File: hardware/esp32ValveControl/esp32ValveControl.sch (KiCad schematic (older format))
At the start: 65 parts, among them Q1 BSS138, Q2 BSS138, Q5 BSS138, Q7 BSS138, SW2 Reset, U1 ESP32-WROOM, U2 AQY212, U3 AQY212, U4 MC34063, U5 MOCD207M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

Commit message: schem_/pcb update
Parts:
- removed D1, D2, D3: LED, LEDs:LED-0603, symbol device:LED
- added C1: 100n, Capacitors_SMD:C_0603, symbol device:C_Small
- added P1: CONN_01X05, Pin_Headers:Pin_Header_Straight_1x05_Pitch2.54mm, symbol conn:CONN_01X05
- added R23: 100, Resistors_SMD:R_0603, symbol device:R
- added SW1: Boot, switches:SMD_Switch_6.5x6, symbol standard:Switch_4P
- added U8: MOCD207M, Housings_SOIC:SOIC-8_3.9x4.9mm_Pitch1.27mm, symbol opto:PC827
- R18, R19, R22, R3, R4, R5: value 470 -> 10k
- R20, R21: value 470 -> tbd
- R8, R9: value 33 -> 10k
- U2, U3, U6, U7: footprint DIP-4-SMD -> Housings_DIP:DIP-4_W7.62mm_SMDSocket_SmallPads
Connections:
- net labels added: IN3, IN4, OPTO3, OPTO4, VCOM, nBoot
- net labels removed: PA12, PA13, PA14, PD6, PD7, PE0, PE1
- wire segments 99 -> 129
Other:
- moved on the sheet: SW2

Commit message: hardware update
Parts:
- removed U5, U8: MOCD207M, Housings_SOIC:SOIC-8_3.9x4.9mm_Pitch1.27mm, symbol opto:PC827
- added U10, U5, U8, U9: LTV-354T, SOIC_Packages:SO-4_4.4x3.6mm_Pitch2.54mm, symbol Isolator:LTV-354T
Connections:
- wire segments 129 -> 137
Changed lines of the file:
@@
-$EndComp
-$Comp
-L opto:PC827 U5
-U 1 1 571AB759
-P 1600 3400
-F 0 "U5" H 1400 3600 50  0000 L CNN
-F 1 "MOCD207M" H 1600 3600 50  0000 L CNN
-F 2 "Housings_SOIC:SOIC-8_3.9x4.9mm_Pitch1.27mm" H 1400 3200 50  0001 L CIN
-F 3 "" H 1600 3400 50  0000 L CNN
-	1    1600 3400
-	1    0    0    -1
-$EndComp
-$Comp
-L opto:PC827 U5
-U 2 1 571AC18A
-P 1600 4050
-F 0 "U5" H 1400 4250 50  0000 L CNN
-F 1 "MOCD207M" H 1600 4250 50  0000 L CNN
-F 2 "Housings_SOIC:SOIC-8_3.9x4.9mm_Pitch1.27mm" H 1400 3850 50  0001 L CIN
-F 3 "" H 1600 4050 50  0000 L CNN
-	2    1600 4050
-	1    0    0    -1
 $EndComp
 $Comp
@@
 	7700 800  7900 800
 Wire Wire Line
-	2000 3950 2100 3950
-Wire Wire Line
 	8050 1550 8050 1900
 $Comp
@@
 Wire Wire Line
 	1900 3300 2000 3300
-Wire Wire Line
-	2000 3300 2100 3300
 Connection ~ 2000 3300
 $Comp
@@
 Wire Wire Line
 	6150 1150 6700 1150
-$Comp
-L opto:PC827 U8
-U 1 1 5B81A865
-P 1600 5000
-F 0 "U8" H 1400 5200 50  0000 L CNN
-F 1 "MOCD207M" H 1600 5200 50  0000 L CNN
-F 2 "Housings_SOIC:SOIC-8_3.9x4.9mm_Pitch1.27mm" H 1400 4800 50  0001 L CIN
-F 3 "" H 1600 5000 50  0000 L CNN
-	1    1600 5000
-	1    0    0    -1
-$EndComp
-$Comp
-L opto:PC827 U8
-U 2 1 5B81A86B
-P 1600 5650
-F 0 "U8" H 1400 5850 50  0000 L CNN
-F 1 "MOCD207M" H 1600 5850 50  0000 L CNN
-F 2 "Housings_SOIC:SOIC-8_3.9x4.9mm_Pitch1.27mm" H 1400 5450 50  0001 L CIN
-F 3 "" H 1600 5650 50  0000 L CNN
-	2    1600 5650
-	1    0    0    -1
-$EndComp
 Text Label 550  4900 0    60   ~ 0
 IN3
@@
 Connection ~ 2000 5550
 Wire Wire Line
-	2000 5550 2100 5550
-Wire Wire Line
 	1900 4900 2000 4900
-Wire Wire Line
-	2000 4900 2100 4900
 Connection ~ 2000 4900
 $Comp
@@
 Text Label 6050 4450 0    60   ~ 0
 CH4
+$Comp
+L Isolator:LTV-354T U5
+U 1 1 5B84B6D3
+P 1600 3400
+F 0 "U5" H 1600 3725 50  0000 C CNN
+F 1 "LTV-354T" H 1600 3634 50  0000 C CNN
+F 2 "SOIC_Packages:SO-4_4.4x3.6mm_Pitch2.54mm" H 1400 3200 50  0001 L CIN
+F 3 "http://optoelectronics.liteon.com/upload/download/DS70-2001-004/S_110_LTV-354T%2020140520.pdf" H 1625 3400 50  0001 L CNN
+	1    1600 3400
+	1    0    0    -1
+$EndComp
+$Comp
+L Isolator:LTV-354T U8
+U 1 1 5B84BAAD
+P 1600 4050
+F 0 "U8" H 1600 4375 50  0000 C CNN
+F 1 "LTV-354T" H 1600 4284 50  0000 C CNN
+F 2 "SOIC_Packages:SO-4_4.4x3.6mm_Pitch2.54mm" H 1400 3850 50  0001 L CIN
+F 3 "http://optoelectronics.liteon.com/upload/download/DS70-2001-004/S_110_LTV-354T%2020140520.pdf" H 1625 4050 50  0001 L CNN
+	1    1600 4050
+	1    0    0    -1
+$EndComp
+$Comp
+L Isolator:LTV-354T U9
+U 1 1 5B84BB59
+P 1600 5000
+F 0 "U9" H 1600 5325 50  0000 C CNN
+F 1 "LTV-354T" H 1600 5234 50  0000 C CNN
+F 2 "SOIC_Packages:SO-4_4.4x3.6mm_Pitch2.54mm" H 1400 4800 50  0001 L CIN
+F 3 "http://optoelectronics.liteon.com/upload/download/DS70-2001-004/S_110_LTV-354T%2020140520.pdf" H 1625 5000 50  0001 L CNN
+	1    1600 5000
+	1    0    0    -1
+$EndComp
+$Comp
+L Isolator:LTV-354T U10
+U 1 1 5B84BC17
+P 1600 5650
+F 0 "U10" H 1600 5975 50  0000 C CNN
+F 1 "LTV-354T" H 1600 5884 50  0000 C CNN
+F 2 "SOIC_Packages:SO-4_4.4x3.6mm_Pitch2.54mm" H 1400 5450 50  0001 L CIN
+F 3 "http://optoelectronics.liteon.com/upload/download/DS70-2001-004/S_110_LTV-354T%2020140520.pdf" H 1625 5650 50  0001 L CNN
+	1    1600 5650
+	1    0    0    -1
+$EndComp
+Wire Wire Line
+	4100 4300 2800 4300
+Wire Wire Line
+	2800 4300 2800 5550
+Wire Wire Line
+	2000 5550 2800 5550
+Wire Wire Line
+	2900 4900 2900 4400
+Wire Wire Line
+	2900 4400 4100 4400
+Wire Wire Line
+	2000 4900 2900 4900
+Wire Wire Line
+	4100 5000 3000 5000
+Wire Wire Line
+	3000 5000 3000 3950
+Wire Wire Line
+	2000 3950 3000 3950
+Wire Wire Line
+	4100 5100 3100 5100
+Wire Wire Line
+	3100 5100 3100 3300
+Wire Wire Line
+	2000 3300 3100 3300
 $EndSCHEMATC

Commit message: libs update
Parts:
- removed D10, D11, D8, D9: TVS, Diodes_SMD:SMA_Standard, symbol device:TVS
- removed D12, D13, D14, D15: LED, LEDs:LED-0603, symbol device:LED
- removed Q1, Q2, Q5, Q7: BSS138, TO_SOT_Packages_SMD:SOT-23, symbol transistors:BSS138
- removed R1, R2, R6, R7: 10k, Resistors_SMD:R_0603, symbol device:R
- removed R33, R34, R35, R36: 470, Resistors_SMD:R_0603, symbol device:R
- removed U2, U3, U6, U7: AQY212, Housings_DIP:DIP-4_W7.62mm_SMDSocket_SmallPads, symbol aqy212:AQY212
- C1, C23, C24, C26, C27: symbol device:C_Small -> esp32ValveControl-rescue:C_Small-device
- C25, C28: symbol device:CP_Small -> esp32ValveControl-rescue:CP_Small-device
- D4, D5: footprint Diodes_SMD:SMA_Standard -> Diodes_SMD:D_SMA; symbol device:D_Schottky -> esp32ValveControl-rescue:D_Schottky-device
- D6: symbol device:D_Small -> esp32ValveControl-rescue:D_Small-device
- D7: footprint Diodes_SMD:SMA_Standard -> Diodes_SMD:D_SMA; symbol device:TVS -> esp32ValveControl-rescue:TVS-device
- F1: symbol device:F_Small -> esp32ValveControl-rescue:F_Small-device
- L9: symbol device:L_Small -> esp32ValveControl-rescue:L_Small-device
- P1: symbol conn:CONN_01X05 -> esp32ValveControl-rescue:CONN_01X05-conn
- R10, R11, R12, R13, R14, R15, R16, R17, R18, R19, R20, R21, R22, R23, R3, R30, R31, R32, R4, R5, R8, R9: symbol device:R -> esp32ValveControl-rescue:R-device
- U4: symbol regul:MC34063 -> esp32ValveControl-rescue:MC34063-regul
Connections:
- wire segments 137 -> 152
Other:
- moved on the sheet: U1, U10, U5, U8, U9

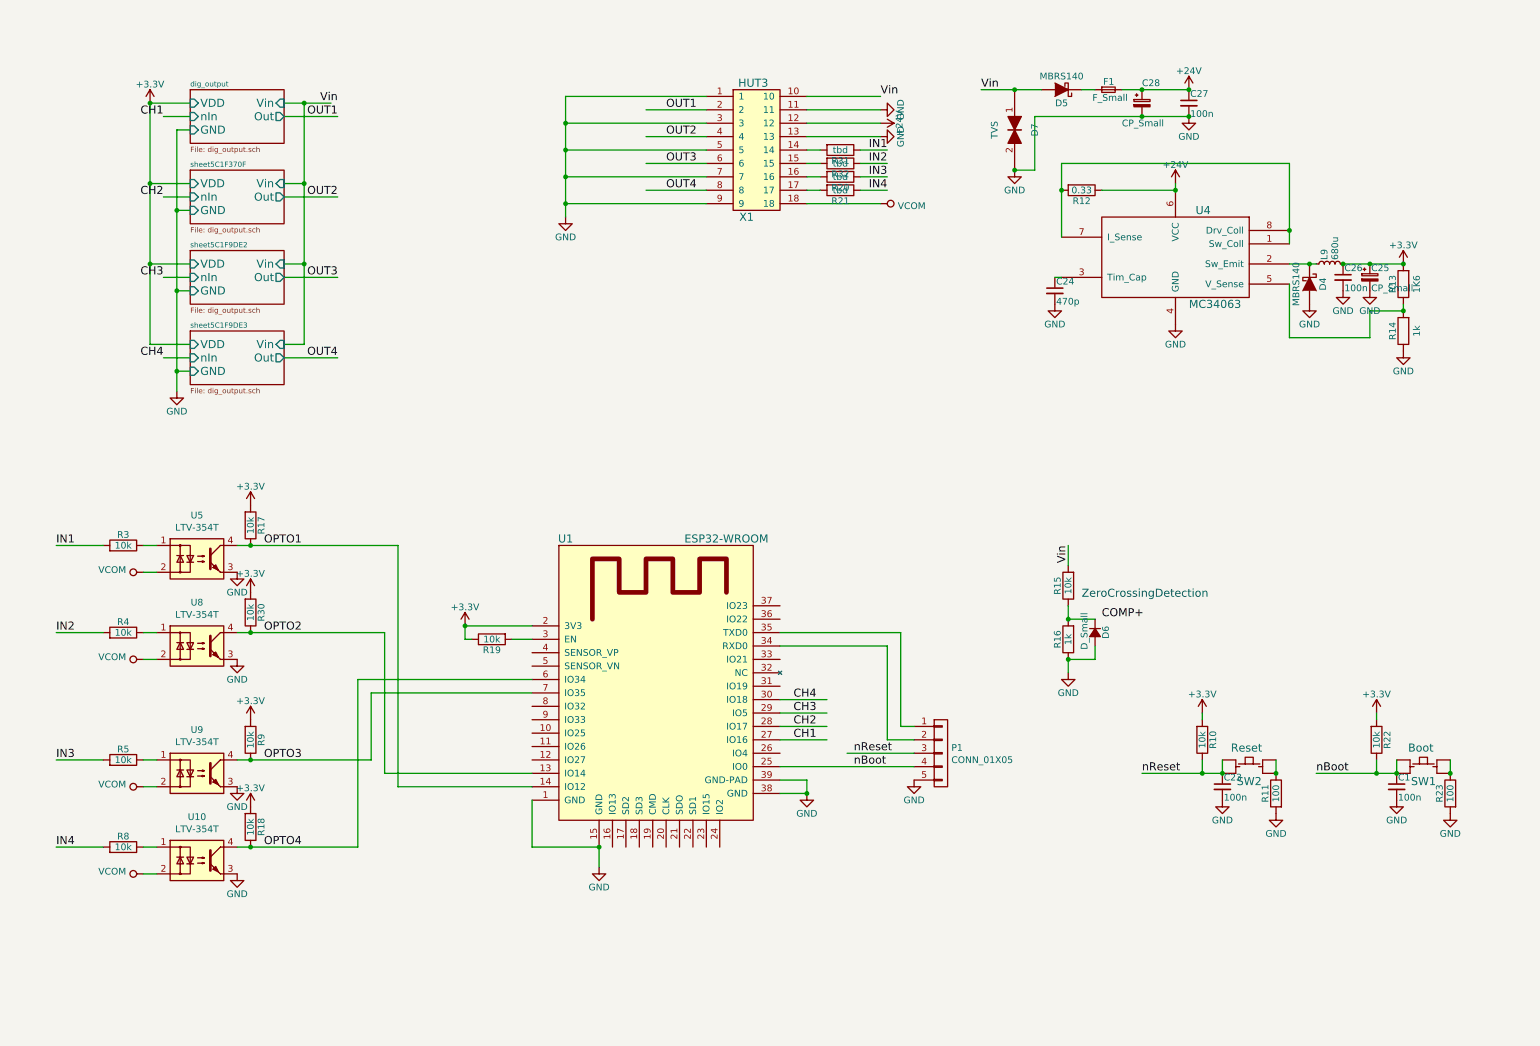
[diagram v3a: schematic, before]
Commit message: hier. schematic updates
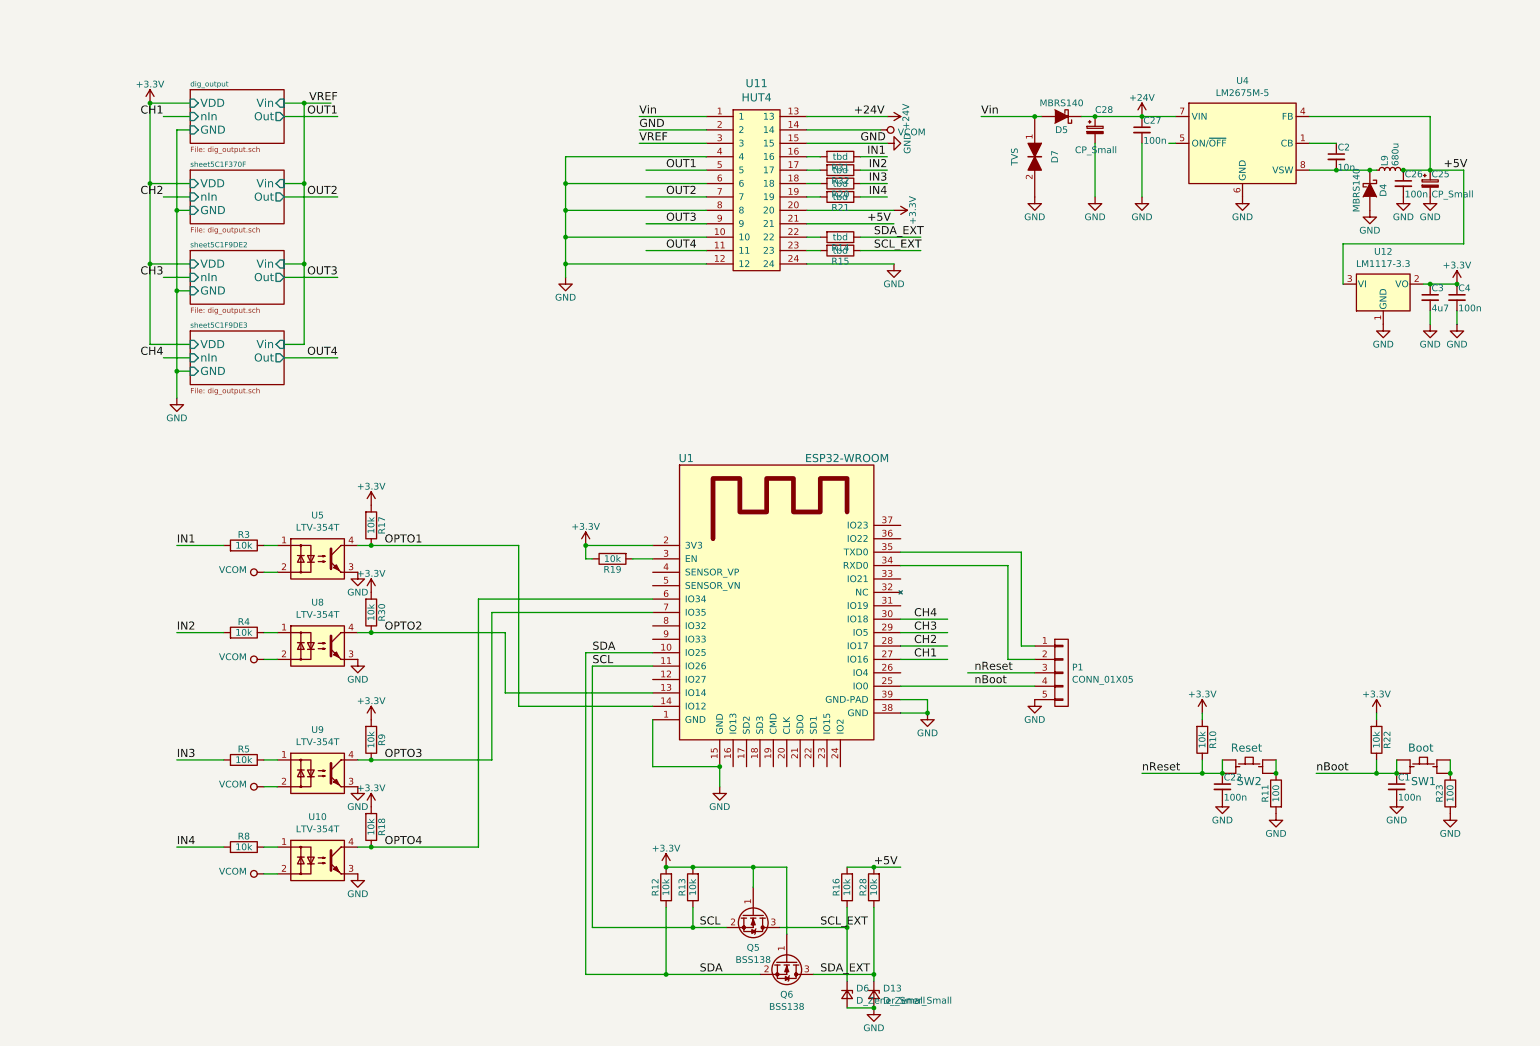
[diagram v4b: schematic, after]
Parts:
- removed C24: 470p, Capacitors_SMD:C_0603, symbol esp32ValveControl-rescue:C_Small-device
- removed D6: D_Small, Diodes_SMD:MiniMELF_Standard, symbol esp32ValveControl-rescue:D_Small-device
- removed F1: F_Small, Fuse_Holders_and_Fuses:Fuse_SMD1206_Wave, symbol esp32ValveControl-rescue:F_Small-device
- removed U4: MC34063, Housings_SOIC:SOIC-8_3.9x4.9mm_Pitch1.27mm, symbol esp32ValveControl-rescue:MC34063-regul
- removed X1: HUT3, cb_hut:CB_HUT_3, symbol hut3:HUT3
- added C2: 10n, Capacitors_SMD:C_0603, symbol esp32ValveControl-rescue:C_Small-device
- added C3: 4u7, Capacitors_SMD:C_0805_HandSoldering, symbol esp32ValveControl-rescue:C_Small-device
- added C4: 100n, Capacitors_SMD:C_0603, symbol esp32ValveControl-rescue:C_Small-device
- added D13, D6: D_Zener_Small, Diodes_SMD:D_SMA, symbol Device:D_Zener_Small
- added Q5, Q6: BSS138, Package_TO_SOT_SMD:SOT-23, symbol Transistor_FET:BSS138
- added R28: 10k, Resistors_SMD:R_0603, symbol esp32ValveControl-rescue:R-device
- added U11: HUT4, cb_hut:CB_HUT_4, symbol hut3:HUT4
- added U12: LM1117-3.3, Package_TO_SOT_SMD:SOT-223-3_TabPin2, symbol Regulator_Linear:LM1117-3.3
- added U4: LM2675M-5, SOIC_Packages:SOIC-8_3.9x4.9mm_Pitch1.27mm, symbol Regulator_Switching:LM2675M-5
- R12: value 0.33 -> 10k; footprint Resistors_SMD:R_1206 -> Resistors_SMD:R_0603
- R13: value 1K6 -> 10k
- R14: value 1k -> tbd
- R15: value 10k -> tbd
- R16: value 1k -> 10k
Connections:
- net labels added: +5V, SCL, SCL_EXT, SDA, SDA_EXT, VREF
- net labels removed: COMP+
- wire segments 152 -> 175
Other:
- note removed: "ZeroCrossingDetection\n"
- moved on the sheet: C25, C26, C27, C28, D4, D5, D7, L9, P1, R17, R18, R19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
